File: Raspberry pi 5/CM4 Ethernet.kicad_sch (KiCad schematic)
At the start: 23 parts, among them J12 MAGJACK-A70-112-331N126, J14 THD-20-R, J15 THD-02-R, J16 Conn_01x03, J17 Conn_01x03, J18 Conn_02x07_Odd_Even, J19 Micro_SD_Card_Det2, U10 RT9742GGJ5, U6 TPD4EUSB30, U7 TPD4EUSB30

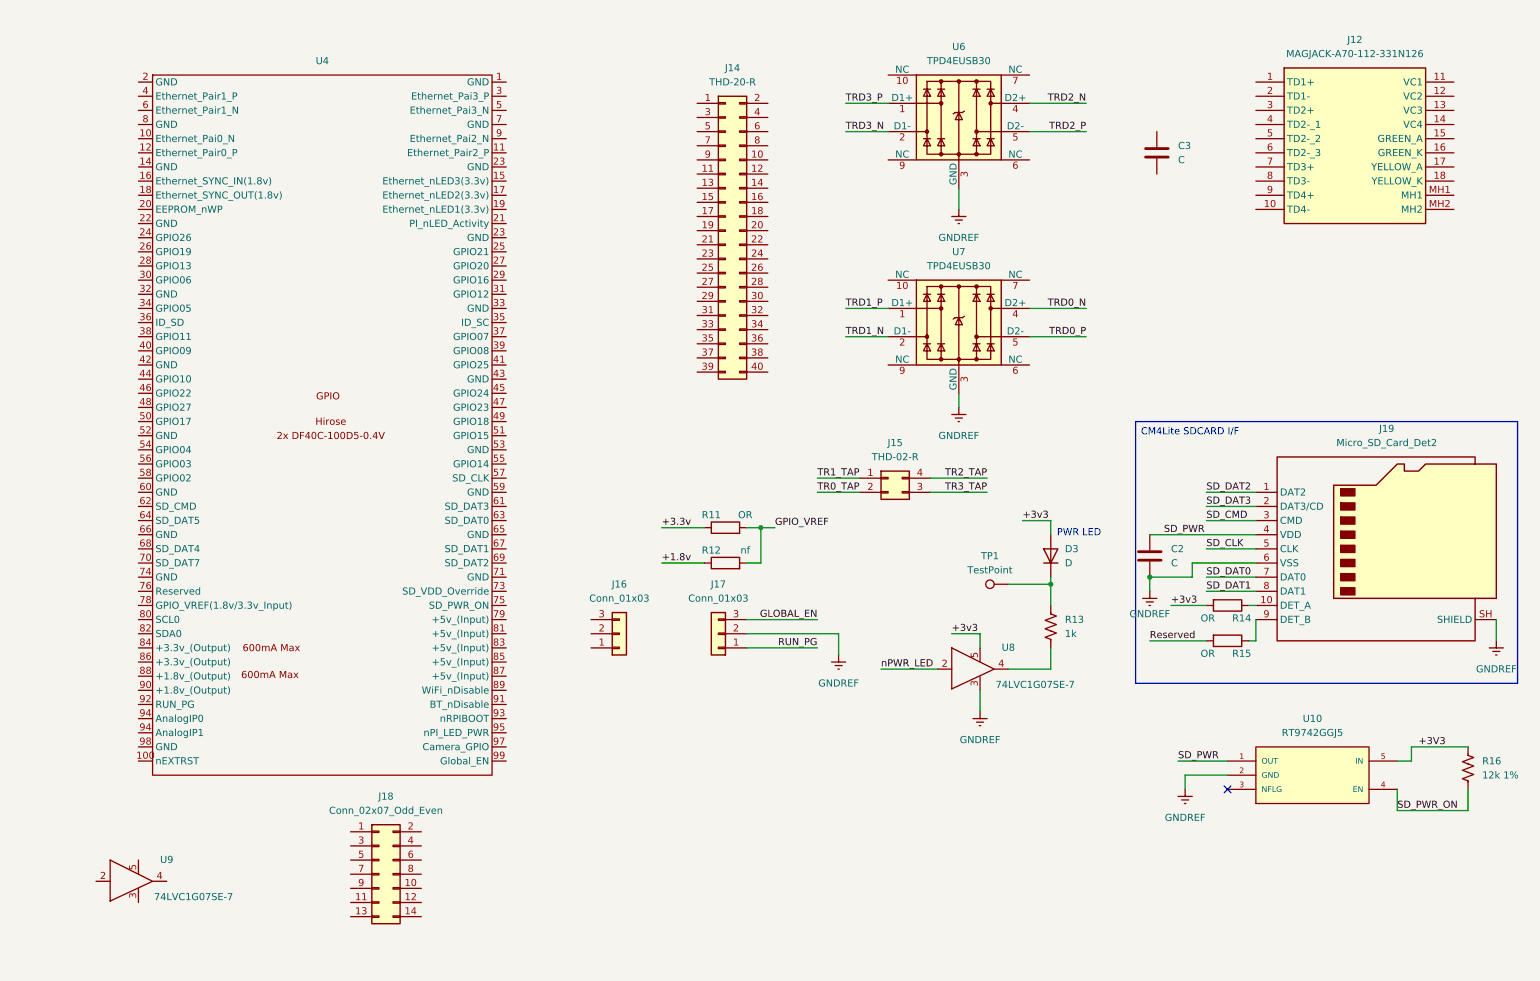
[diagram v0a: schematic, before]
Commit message: 繪製CM4 Enternet
進度達1/3
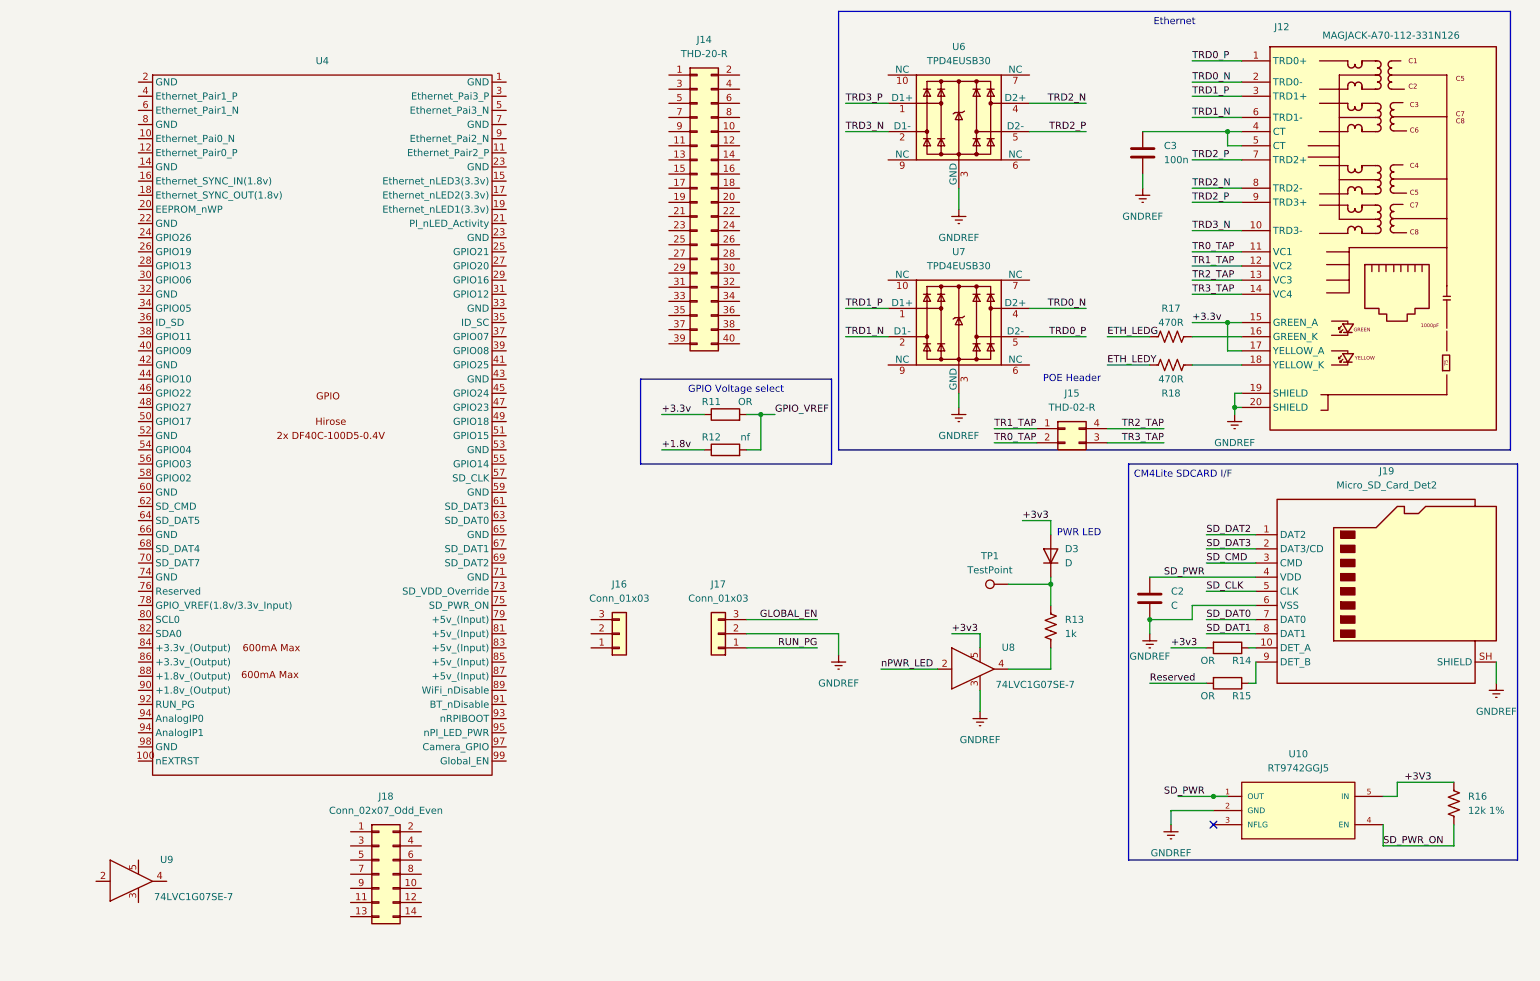
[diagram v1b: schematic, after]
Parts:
- added R17, R18: 470R, symbol Device:R_US
- C3: value C -> 100n
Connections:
- net +3.3v: now also J12.15 (GREEN_A), J12.17 (YELLOW_A)
- net GNDREF: now also C3.2, J12.19 (SHIELD), J12.20 (SHIELD)
- net SD_PWR: no longer U10.1 (OUT)
- net TR0_TAP: now also J12.11 (VC1)
- net TR1_TAP: now also J12.12 (VC2)
- net TR2_TAP: now also J12.13 (VC3)
- net TR3_TAP: now also J12.14 (VC4)
- net TRD0_N: now also J12.2 (TRD0-)
- net TRD0_P: now also J12.1 (TRD0+)
- net TRD1_N: now also J12.6 (TRD1-)
- net TRD1_P: now also J12.3 (TRD1+)
- net TRD2_N: now also J12.8 (TRD2-)
- net TRD2_P: now also J12.7 (TRD2+), J12.9 (TRD3+)
- net TRD3_N: now also J12.10 (TRD3-)
- net at C3.1: now also J12.4 (CT), J12.5 (CT)
- net at J12.16 (GREEN_K): now also R17.2
- net at J12.18 (YELLOW_K): now also R18.1
- new net ETH_LEDG: R17.1
- new net ETH_LEDY: R18.2
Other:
- note added: "POE Header"
- moved on the sheet: C2, C3, J14, J15, J19, R11, R12, R14, R15, R16, U10

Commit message: update the Ethernet IO Board
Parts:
- added D4: LED Green, symbol Device:D
- added R19: 1k, symbol Device:R_US
- added TP2: TestPoint, symbol Connector:TestPoint
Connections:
- net +1.8v: now also U4.88 (+1.8v_(Output)), U4.90 (+1.8v_(Output))
- net +3.3v: now also J14.1 (Pin_1), J14.17 (Pin_17), U4.84 (+3.3v_(Output)), U4.86 (+3.3v_(Output))
- net +3v3: now also D4.2 (A)
- net ETH_LEDG: now also U4.17 (Ethernet_nLED2(3.3v))
- net ETH_LEDY: now also U4.15 (Ethernet_nLED3(3.3v))
- net GLOBAL_EN: now also J18.14 (Pin_14), U4.99 (Global_EN)
- net GNDREF: now also J14.14 (Pin_14), J14.20 (Pin_20), J14.25 (Pin_25), J14.30 (Pin_30), J14.34 (Pin_34), J14.39 (Pin_39), J14.6 (Pin_6), J14.9 (Pin_9), J16.2 (Pin_2), U4.1 (GND), U4.13 (GND), U4.14 (GND), U4.2 (GND), U4.22 (GND), U4.23 (GND), U4.32 (GND), U4.33 (GND), U4.42 (GND), U4.43 (GND), U4.52 (GND), U4.53 (GND), U4.59 (GND), U4.60 (GND), U4.65 (GND), U4.66 (GND), U4.7 (GND), U4.71 (GND), U4.74 (GND), U4.8 (GND), U4.98 (GND), U9.3
- net GPIO_VREF: now also U4.78 (GPIO_VREF(1.8v/3.3v_Input))
- net RUN_PG: now also U4.92 (RUN_PG), U9.2
- net Reserved: now also U4.76 (Reserved)
- net SD_CLK: now also U4.57 (SD_CLK)
- net SD_CMD: now also U4.62 (SD_CMD)
- net SD_DAT0: now also U4.63 (SD_DAT0)
- net SD_DAT1: now also U4.67 (SD_DAT1)
- net SD_DAT2: now also U4.69 (SD_DAT2)
- net SD_DAT3: now also U4.61 (SD_DAT3)
- net SD_PWR_ON: now also U4.75 (SD_PWR_ON)
- net TRD0_N: now also U4.12 (Ethernet_Pair0_P)
- net TRD0_P: now also U4.10 (Ethernet_Pair0_N)
- net TRD1_N: now also U4.20 (EEPROM_nWP), U4.6 (Ethernet_Pair1_N)
- net TRD1_P: now also U4.4 (Ethernet_Pair1_P)
- net TRD2_N: now also U4.11 (Ethernet_Pair2_P)
- net TRD2_P: now also U4.9 (Ethernet_Pair2_N)
- net TRD3_N: now also U4.5 (Ethernet_Pair3_N)
- net TRD3_P: now also U4.3 (Ethernet_Pair3_P)
- net nPWR_LED: now also U4.95 (nPI_LED_PWR)
- net at U9.4: now also J18.13 (Pin_13)
- net +5v: now reaches U9.5
- net +5v: now also J14.2 (Pin_2), J14.4 (Pin_4), U4.77 (+5v_(Input)), U4.79 (+5v_(Input)), U4.81 (+5v_(Input)), U4.83 (+5v_(Input)), U4.85 (+5v_(Input)), U4.87 (+5v_(Input))
- net WL_nDis: now reaches J16.1 (Pin_1)
- net WL_nDis: now also U4.89 (WiFi_nDisable)
- net BT_nDis: now reaches J16.3 (Pin_3)
- net BT_nDis: now also U4.91 (BT_nDisable)
- net GND: now reaches J18.1 (Pin_1)
- net GND: now also J18.10 (Pin_10), J18.12 (Pin_12), J18.3 (Pin_3), J18.7 (Pin_7)
- net TV_OUT: now reaches J18.11 (Pin_11)
- net nRPIBOOT: now reaches J18.2 (Pin_2)
- net nRPIBOOT: now also U4.93 (nRPIBOOT)
- net EEPROM_nWP: now reaches J18.4 (Pin_4)
- net AINO: now reaches J18.5 (Pin_5)
- net AIN1: now reaches J18.6 (Pin_6)
- net AIN1: now also U4.94 (AnalogIP1)
- net SYNC_IN: now reaches J18.8 (Pin_8)
- net SYNC_IN: now also U4.16 (Ethernet_SYNC_IN(1.8v))
- net SYNC_OUT: now reaches J18.9 (Pin_9)
- net SYNC_OUT: now also U4.18 (Ethernet_SYNC_OUT(1.8v))
- net nEXTRST: now reaches U4.100 (nEXTRST)
- net at U4.21 (PI_nLED_Activity): now also R19.2
- net GPIO26: now reaches U4.24 (GPIO26)
- net GPIO26: now also J14.37 (Pin_37), U4.44 (GPIO10)
- net GPIO21: now reaches U4.25 (GPIO21)
- net GPIO21: now also J14.40 (Pin_40)
- net GPIO19: now reaches U4.26 (GPIO19)
- net GPIO19: now also J14.35 (Pin_35), U4.46 (GPIO22)
- net GPIO20: now reaches U4.27 (GPIO20)
- net GPIO20: now also J14.38 (Pin_38)
- net GPIO13: now reaches U4.28 (GPIO13)
- net GPIO13: now also J14.33 (Pin_33), U4.48 (GPIO27)
- net GPIO16: now reaches U4.29 (GPIO16)
- net GPIO16: now also J14.36 (Pin_36)
- net GPIO06: now reaches U4.30 (GPIO06)
- net GPIO06: now also J14.31 (Pin_31), U4.50 (GPIO17)
- net GPIO12: now reaches U4.31 (GPIO12)
- net GPIO12: now also J14.32 (Pin_32)
- net GPIO05: now reaches U4.34 (GPIO05)
- net GPIO05: now also J14.29 (Pin_29)
- net ID_SC: now reaches U4.35 (ID_SC)
- net ID_SC: now also J14.28 (Pin_28)
- net ID_SD: now reaches U4.36 (ID_SD)
- net ID_SD: now also J14.27 (Pin_27)
- net GPIO07: now reaches U4.37 (GPIO07)
- net GPIO07: now also J14.26 (Pin_26)
- net GPIO11: now reaches U4.38 (GPIO11)
- net GPIO11: now also J14.23 (Pin_23)
- net GPIO08: now reaches U4.39 (GPIO08)
- net GPIO08: now also J14.24 (Pin_24)
- net GPIO09: now reaches U4.40 (GPIO09)
- net GPIO09: now also J14.21 (Pin_21)
- net GPIO25: now reaches U4.41 (GPIO25)
- net GPIO25: now also J14.22 (Pin_22)
- net GPIO24: now reaches U4.45 (GPIO24)
- net GPIO24: now also J14.18 (Pin_18)
- net GPIO23: now reaches U4.47 (GPIO23)
- net GPIO23: now also J14.16 (Pin_16)
- net GPIO18: now reaches U4.49 (GPIO18)
- net GPIO18: now also J14.12 (Pin_12)
- net GPIO15: now reaches U4.51 (GPIO15)
- net GPIO15: now also J14.10 (Pin_10)
- net GPIO04: now reaches U4.54 (GPIO04)
- net GPIO04: now also J14.7 (Pin_7)
- net GPIO14: now reaches U4.55 (GPIO14)
- net GPIO14: now also J14.8 (Pin_8)
- net GPIO03: now reaches U4.56 (GPIO03)
- net GPIO03: now also J14.5 (Pin_5)
- net GPIO02: now reaches U4.58 (GPIO02)
- net GPIO02: now also J14.3 (Pin_3)
- net SCL0: now reaches U4.80 (SCL0)
- net SDA0: now reaches U4.82 (SDA0)
- net CAM_GPIO: now reaches U4.97 (Camera_GPIO)
- net GPIO17: now reaches J14.11 (Pin_11)
- net GPIO27: now reaches J14.13 (Pin_13)
- net GPIO22: now reaches J14.15 (Pin_15)
- net GPIO10: now reaches J14.19 (Pin_19)
- new net: D4.1 (K), R19.1, TP2.1
- new net AIN0: U4.96 (AnalogIP0)
- no-connect marks 1 -> 7
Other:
- note added: "A button bwteen pins 13-14 can be used to wake up compute moudle from power down If compute modules is awake RUN_PG will be high so the button doesn't do anything If the compute module is asleep the RUN_PG will be at 0v and so pull global enable low"
- note added: "Activiy LED"
- note added: "Ethernet POE Protection"
- note added: "Force RPIBOOT = Jumper Pins 1-2 EEPROM write protect = Jumper Pins 3-4"
- note added: "Not Fitted headers"
- title: (none) -> Compute Module 4 IO Board - GPIO - Ethernet
- moved on the sheet: J14, J16, J17, J18, R11, R12, U6, U7
